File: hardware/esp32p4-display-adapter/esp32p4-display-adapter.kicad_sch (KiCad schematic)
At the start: 5 parts, among them J1 ESP32-P4_DSI_22pin, J2 Display_30pin, U1 AP2127K-2.8, U2 AP2127K-1.8, U3 TXB0102

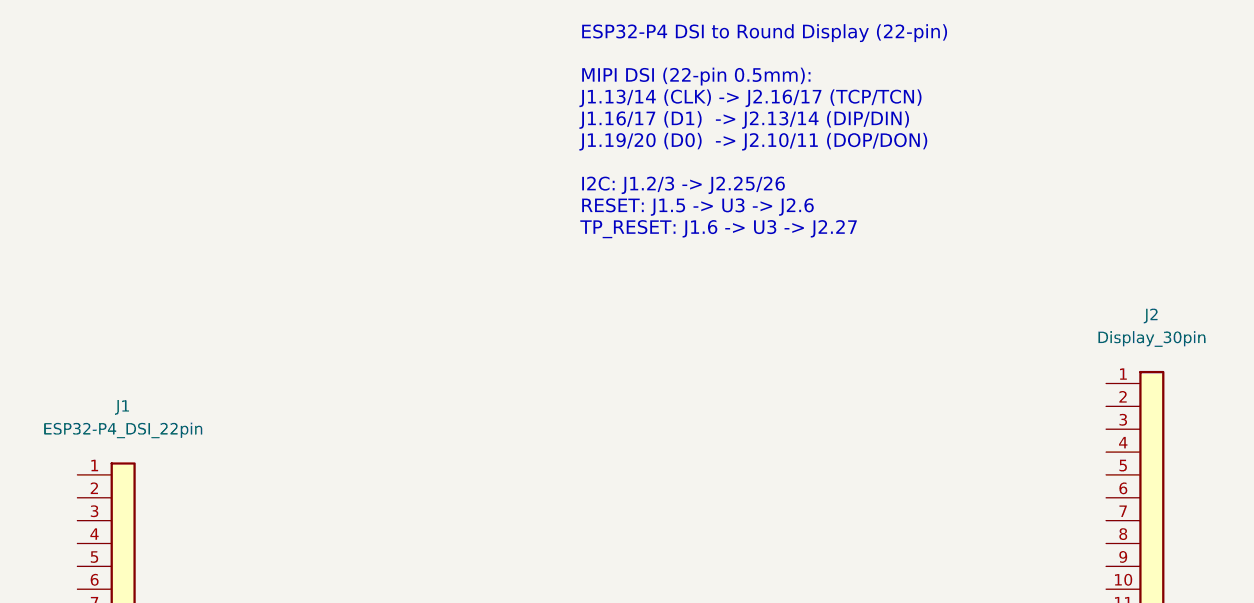
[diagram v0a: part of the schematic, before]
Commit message: Restore esp32p4-display-adapter (22-pin), add esp32p4-display-adapter-15pin
- esp32p4-display-adapter: 22-pin 0.5mm (your working version restored)
- esp32p4-display-adapter-15pin: NEW - 15-pin 1.0mm (same pinout as RPi)
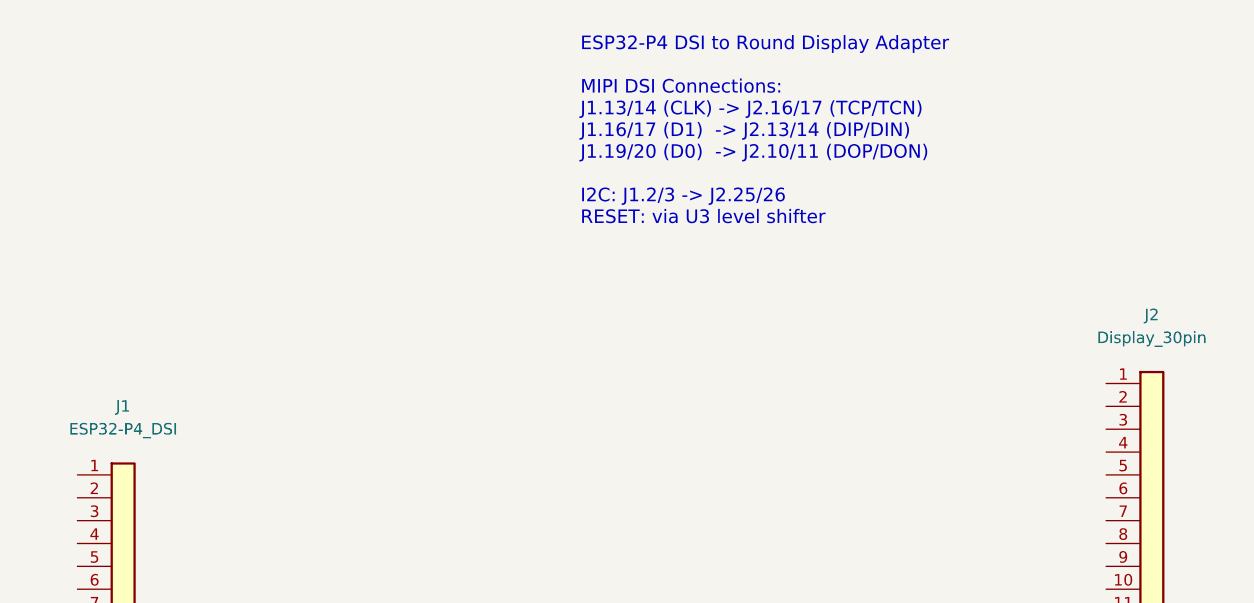
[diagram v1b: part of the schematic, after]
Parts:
- J1: value ESP32-P4_DSI_22pin -> ESP32-P4_DSI
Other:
- note added: "ESP32-P4 DSI to Round Display Adapter MIPI DSI Connections: J1.13/14 (CLK) -> J2.16/17 (TCP/TCN) J1.16/17 (D1) -> J2.13/14 (DIP/DIN) J1.19/20 (D0) -> J2.10/11 (DOP/DON) I2C: J1.2/3 -> J2.25/26 RESET: via U3 level shifter"
- note removed: "ESP32-P4 DSI to Round Display (22-pin) MIPI DSI (22-pin 0.5mm): J1.13/14 (CLK) -> J2.16/17 (TCP/TCN) J1.16/17 (D1) -> J2.13/14 (DIP/DIN) J1.19/20 (D0) -> J2.10/11 (DOP/DON) I2C: J1.2/3 -> J2.25/26 RESET: J1.5 -> U3 -> J2.6 TP_RESET: J1.6 -> U3 -> J2.27"
- title: ESP32-P4 DSI to Round Display Adapter (22-pin) -> ESP32-P4 DSI to Round Display Adapter
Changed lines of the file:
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@@
   (paper "A4")
   (title_block
-    (title "ESP32-P4 DSI to Round Display Adapter (22-pin)")
+    (title "ESP32-P4 DSI to Round Display Adapter")
     (date "2026-04-24")
     (rev "1.0")
@@
     (dnp no)
     (property "Reference" "J1" (at 38.1 55.88 0) (effects (font (size 1.27 1.27))))
-    (property "Value" "ESP32-P4_DSI_22pin" (at 38.1 58.42 0) (effects (font (size 1.27 1.27))))
+    (property "Value" "ESP32-P4_DSI" (at 38.1 58.42 0) (effects (font (size 1.27 1.27))))
     (property "Footprint" "Connector_FFC-FPC:Hirose_FH12-22S-0.5SH_1x22-1MP_P0.50mm_Horizontal" (at 38.1 88.9 0) (effects (font (size 1.27 1.27)) hide))
     (pin "1")
@@
     (pin "22")
     (instances
-      (project "esp32p4-display-adapter-22pin"
-        (path "/c3d4e5f6-a7b8-9012-cdef-345678901234" (reference "J1") (unit 1))
+      (project "esp32p4-display-adapter"
+        (path "/a1b2c3d4-e5f6-7890-abcd-ef1234567890" (reference "J1") (unit 1))
       )
     )
@@
     (pin "30")
     (instances
-      (project "esp32p4-display-adapter-22pin"
-        (path "/c3d4e5f6-a7b8-9012-cdef-345678901234" (reference "J2") (unit 1))
+      (project "esp32p4-display-adapter"
+        (path "/a1b2c3d4-e5f6-7890-abcd-ef1234567890" (reference "J2") (unit 1))
       )
     )
@@
     (pin "5")
     (instances
-      (project "esp32p4-display-adapter-22pin"
-        (path "/c3d4e5f6-a7b8-9012-cdef-345678901234" (reference "U1") (unit 1))
+      (project "esp32p4-display-adapter"
+        (path "/a1b2c3d4-e5f6-7890-abcd-ef1234567890" (reference "U1") (unit 1))
       )
     )
@@
     (pin "5")
     (instances
-      (project "esp32p4-display-adapter-22pin"
-        (path "/c3d4e5f6-a7b8-9012-cdef-345678901234" (reference "U2") (unit 1))
+      (project "esp32p4-display-adapter"
+        (path "/a1b2c3d4-e5f6-7890-abcd-ef1234567890" (reference "U2") (unit 1))
       )
     )
@@
     (pin "8")
     (instances
-      (project "esp32p4-display-adapter-22pin"
-        (path "/c3d4e5f6-a7b8-9012-cdef-345678901234" (reference "U3") (unit 1))
+      (project "esp32p4-display-adapter"
+        (path "/a1b2c3d4-e5f6-7890-abcd-ef1234567890" (reference "U3") (unit 1))
       )
     )
   )
-  (text "ESP32-P4 DSI to Round Display (22-pin)\n\nMIPI DSI (22-pin 0.5mm):\nJ1.13/14 (CLK) -> J2.16/17 (TCP/TCN)\nJ1.16/17 (D1)  -> J2.13/14 (DIP/DIN)\nJ1.19/20 (D0)  -> J2.10/11 (DOP/DON)\n\nI2C: J1.2/3 -> J2.25/26\nRESET: J1.5 -> U3 -> J2.6\nTP_RESET: J1.6 -> U3 -> J2.27"
+  (text "ESP32-P4 DSI to Round Display Adapter\n\nMIPI DSI Connections:\nJ1.13/14 (CLK) -> J2.16/17 (TCP/TCN)\nJ1.16/17 (D1)  -> J2.13/14 (DIP/DIN)\nJ1.19/20 (D0)  -> J2.10/11 (DOP/DON)\n\nI2C: J1.2/3 -> J2.25/26\nRESET: via U3 level shifter"
     (exclude_from_sim no)
     (at 88.9 25.4 0)
